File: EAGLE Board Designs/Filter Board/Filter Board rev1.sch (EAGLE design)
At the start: 9 parts, among them U1 MAX7400

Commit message: progress
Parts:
- removed U1: MAX7400, HyTechDevices:MAX7400
- added C2: CAPACITOR_0603_25V_47NF, HyTechDevices:CAPACITOR_0603_25V_47NF
- added J4, J5: CONNECTOR-40__, HyTechDevices:CONNECTOR-40__
- added R5: RESISTOR_0603_3.3K, HyTechDevices:RESISTOR_0603_3.3K
- C1: value CAPACITOR_0603_10V_680PF -> CAPACITOR_0603_25V_47NF; device HyTechDevices:CAPACITOR_0603_10V_680PF -> HyTechDevices:CAPACITOR_0603_25V_47NF
- C3: value (none) -> CAPACITOR_0603_25V_47NF; device HyTechSymbols:CAPACITOR -> HyTechDevices:CAPACITOR_0603_25V_47NF
- C5: value CAPACITOR_0603_10V_0.1UF -> CAPACITOR_0603_25V_47NF; device HyTechDevices:CAPACITOR_0603_10V_0.1UF -> HyTechDevices:CAPACITOR_0603_25V_47NF
- R1: value (none) -> RESISTOR_0603_3.3K; device HyTechSymbols:RESISTOR -> HyTechDevices:RESISTOR_0603_3.3K
- R2: value RESISTOR_0603_13K -> RESISTOR_0603_3.3K; device HyTechDevices:RESISTOR_0603_13K -> HyTechDevices:RESISTOR_0603_3.3K
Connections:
- removed net FILTERED_FREQ: C3.1, R1.2
- removed net INPUT_SIGNAL: U1.IN
- removed net N$3: C1.1, U1.CLK
- removed net N$4: C5.1, U1.COM, U1.OS
- removed net OUTPUT_SIGNAL: U1.OUT
- removed net RAW_24V_SIGNAL: R2.1
- removed net REGULATED_SIGNAL: R2.2, R3.1
- new net ACCEL_1: J5.5
- new net ACCEL_1_EXT: J5.3
- new net ACCEL_2: J5.9
- new net ACCEL_2_EXT: J5.7
- new net BRAKE_1: J5.13
- new net BRAKE_1_EXT: J5.11
- new net BRAKE_2: J5.17
- new net BRAKE_2_EXT: J5.15
- new net BRAKE_PRESSURE_F: C2.1, J5.28, R2.2
- new net BRAKE_PRESSURE_F_EXT: J5.27, R2.1
- new net BRAKE_PRESSURE_R: C3.1, J5.30, R3.2
- new net BRAKE_PRESSURE_R_EXT: J5.29, R3.1
- new net CURRENT: J5.34
- new net CURRENT_EXT: J5.32
- new net LOAD_FL: J4.5
- new net LOAD_FL_EXT: J4.3
- new net LOAD_FR: J4.9
- new net LOAD_FR_EXT: J4.7
- new net LOAD_RL: J4.13
- new net LOAD_RL_EXT: J4.11
- new net LOAD_RR: J4.17
- new net LOAD_RR_EXT: J4.15
- new net REFERENCE: J5.38
- new net REFERENCE_EXT: J5.36
- new net SPN_POT_1: J4.21
- new net SPN_POT_1_EXT: J4.19
- new net SPN_POT_2: J4.25
- new net SPN_POT_2_EXT: J4.23
- new net SPN_POT_3: J4.29
- new net SPN_POT_3_EXT: J4.27
- new net SPN_POT_4: J4.33
- new net SPN_POT_4_EXT: J4.31
- new net SPN_POT_5: J4.37
- new net SPN_POT_5_EXT: J4.35
- new net SPN_POT_6: J5.1
- new net SPN_POT_6_EXT: J4.39
- new net STEERING_1: C5.1, J5.21, R5.2
- new net STEERING_1_EXT: J5.19, R5.1
- new net STEERING_2: C1.1, J5.25, R1.2
- new net STEERING_2_EXT: J5.23, R1.1
- net +5V: now also J4.1; no longer U1.!SHDN, U1.VDD
- net GND: now also C2.2, J4.10, J4.12, J4.14, J4.16, J4.18, J4.2, J4.20, J4.22, J4.24, J4.26, J4.28, J4.30, J4.32, J4.34, J4.36, J4.38, J4.4, J4.6, J4.8, J5.10, J5.12, J5.14, J5.16, J5.18, J5.2, J5.20, J5.22, J5.24, J5.26, J5.31, J5.33, J5.35, J5.37, J5.4, J5.6, J5.8; no longer R3.2, U1.GND
- net REGULATED_FREQ: no longer R1.1
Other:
- moved on the sheet: C1, C3, C5, C6, C7, R1, R2, R3

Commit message: Prototype filter schematic
my eagle is scuffed :(
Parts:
- added C10, C14, C18, C22, C58, C62, C66, C70, C74, C78: CAPACITOR_0603_10V_1UF, HyTechDevices:CAPACITOR_0603_10V_1UF
- added C11, C13, C15, C17, C19, C21, C23, C4, C55, C57, C59, C61, C63, C65, C67, C69, C71, C73, C75, C77, C79, C9: CAPACITOR_0603_10V_0.1UF, HyTechDevices:CAPACITOR_0603_10V_0.1UF
- added C12, C16, C20, C24, C56, C60, C64, C68, C72, C76, C8, C80: CAPACITOR_0603_10V_680PF, HyTechDevices:CAPACITOR_0603_10V_680PF
- added C49, C50, C51, C52, C53, C54: CAPACITOR_0603_25V_47NF, HyTechDevices:CAPACITOR_0603_25V_47NF
- added R10, R12, R14, R16, R18, R19, R20, R21, R22, R23, R24, R26, R30, R32, R34, R6, R8: RESISTOR_0603_3.3K, HyTechDevices:RESISTOR_0603_3.3K
- added R11, R13, R15, R17, R25, R29, R31, R33, R4, R7, R9: RESISTOR_0603_13K, HyTechDevices:RESISTOR_0603_13K
- added U1, U12, U13, U14, U15, U16, U17, U18, U2, U3, U4, U5: MAX7400, HyTechDevices:MAX7400
- C1: value CAPACITOR_0603_25V_47NF -> CAPACITOR_0603_10V_0.1UF; device HyTechDevices:CAPACITOR_0603_25V_47NF -> HyTechDevices:CAPACITOR_0603_10V_0.1UF
- C5: value CAPACITOR_0603_25V_47NF -> CAPACITOR_0603_10V_1UF; device HyTechDevices:CAPACITOR_0603_25V_47NF -> HyTechDevices:CAPACITOR_0603_10V_1UF
- R1: value RESISTOR_0603_3.3K -> RESISTOR_0603_13K; device HyTechDevices:RESISTOR_0603_3.3K -> HyTechDevices:RESISTOR_0603_13K
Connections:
- new net CURRENT_EXT_5V: R1.2, R5.1, U18.IN
- new net GND1: R12.2, R16.2
- new net GND2: R14.2, R18.2, R26.2, R5.2
- new net LOAD_FL_EXT_5V: R29.2, R30.1, U2.IN
- new net LOAD_FR_EXT_5V: R7.2, R8.1, U3.IN
- new net LOAD_RL_EXT_5V: R31.2, R32.1, U4.IN
- new net LOAD_RR_EXT_5V: R33.2, R34.1, U5.IN
- new net N$10: C19.1, U4.COM, U4.OS
- new net N$11: C24.1, U5.CLK
- new net N$12: C23.1, U5.COM, U5.OS
- new net N$25: C56.1, U12.CLK
- new net N$26: C55.1, U12.COM, U12.OS
- new net N$27: C64.1, U14.CLK
- new net N$28: C63.1, U14.COM, U14.OS
- new net N$29: C60.1, U13.CLK
- new net N$3: C8.1, U1.CLK
- new net N$30: C59.1, U13.COM, U13.OS
- new net N$31: C72.1, U16.CLK
- new net N$32: C71.1, U16.COM, U16.OS
- new net N$33: C68.1, U15.CLK
- new net N$34: C67.1, U15.COM, U15.OS
- new net N$35: C80.1, U18.CLK
- new net N$36: C79.1, U18.COM, U18.OS
- new net N$37: C76.1, U17.CLK
- new net N$38: C75.1, U17.COM, U17.OS
- new net N$4: C4.1, U1.COM, U1.OS
- new net N$5: C12.1, U2.CLK
- new net N$6: C11.1, U2.COM, U2.OS
- new net N$7: C16.1, U3.CLK
- new net N$8: C15.1, U3.COM, U3.OS
- new net N$9: C20.1, U4.CLK
- new net REFERENCE_EXT_5V: R25.2, R26.1, U1.IN
- new net SPN_POT_1_EXT_5V: R10.1, R22.1, R9.2
- new net SPN_POT_2_EXT_5V: R23.1, R4.2, R6.1
- new net SPN_POT_3_EXT_5V: R15.2, R16.1, R24.1
- new net SPN_POT_4_EXT_5V: R17.2, R18.1, R19.1
- new net SPN_POT_5_EXT_5V: R11.2, R12.1, R20.1
- new net SPN_POT_6_EXT_5V: R13.2, R14.1, R21.1
- net +5V: now also U1.!SHDN, U1.VDD, U12.!SHDN, U12.VDD, U13.!SHDN, U13.VDD, U14.!SHDN, U14.VDD, U15.!SHDN, U15.VDD, U16.!SHDN, U16.VDD, U17.!SHDN, U17.VDD, U18.!SHDN, U18.VDD, U2.!SHDN, U2.VDD, U3.!SHDN, U3.VDD, U4.!SHDN, U4.VDD, U5.!SHDN, U5.VDD
- net ACCEL_1: now also U12.OUT
- net ACCEL_1_EXT: now also U12.IN
- net ACCEL_2: now also U13.OUT
- net ACCEL_2_EXT: now also U13.IN
- net BRAKE_1: now also U14.OUT
- net BRAKE_1_EXT: now also U14.IN
- net BRAKE_2: now also U15.OUT
- net BRAKE_2_EXT: now also U15.IN
- net CURRENT: now also U18.OUT
- net CURRENT_EXT: now also R1.1
- net GND: now also C10.2, C11.2, C12.2, C13.2, C14.2, C15.2, C16.2, C17.2, C18.2, C19.2, C20.2, C21.2, C22.2, C23.2, C24.2, C4.2, C49.2, C50.2, C51.2, C52.2, C53.2, C54.2, C55.2, C56.2, C57.2, C58.2, C59.2, C60.2, C61.2, C62.2, C63.2, C64.2, C65.2, C66.2, C67.2, C68.2, C69.2, C70.2, C71.2, C72.2, C73.2, C74.2, C75.2, C76.2, C77.2, C78.2, C79.2, C8.2, C80.2, C9.2, R10.2, R30.2, R32.2, R34.2, R6.2, R8.2, U1.GND, U12.GND, U13.GND, U14.GND, U15.GND, U16.GND, U17.GND, U18.GND, U2.GND, U3.GND, U4.GND, U5.GND
- net LOAD_FL: now also U2.OUT
- net LOAD_FL_EXT: now also R29.1
- net LOAD_FR: now also U3.OUT
- net LOAD_FR_EXT: now also R7.1
- net LOAD_RL: now also U4.OUT
- net LOAD_RL_EXT: now also R31.1
- net LOAD_RR: now also U5.OUT
- net LOAD_RR_EXT: now also R33.1
- net REFERENCE: now also U1.OUT
- net REFERENCE_EXT: now also R25.1
- net REGULATED_FREQ: now also C1.1, C10.1, C13.1, C14.1, C17.1, C18.1, C21.1, C22.1, C5.1, C57.1, C58.1, C61.1, C62.1, C65.1, C66.1, C69.1, C70.1, C73.1, C74.1, C77.1, C78.1, C9.1
- net SPN_POT_1: now also C52.1, R22.2
- net SPN_POT_1_EXT: now also R9.1
- net SPN_POT_2: now also C53.1, R23.2
- net SPN_POT_2_EXT: now also R4.1
- net SPN_POT_3: now also C54.1, R24.2
- net SPN_POT_3_EXT: now also R15.1
- net SPN_POT_4: now also C49.1, R19.2
- net SPN_POT_4_EXT: now also R17.1
- net SPN_POT_5: now also C50.1, R20.2
- net SPN_POT_5_EXT: now also R11.1
- net SPN_POT_6: now also C51.1, R21.2
- net SPN_POT_6_EXT: now also R13.1
- net STEERING_1: now also U16.OUT; no longer C5.1, R5.2
- net STEERING_1_EXT: now also U16.IN; no longer R5.1
- net STEERING_2: now also U17.OUT; no longer C1.1, R1.2
- net STEERING_2_EXT: now also U17.IN; no longer R1.1

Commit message: Updated Filter Board Schematic
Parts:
- added C100, C104, C28, C32, C36, C40, C44, C48, C84, C88, C92, C96: CAPACITOR_0603_10V_680PF, HyTechDevices:CAPACITOR_0603_10V_680PF
- added C101, C103, C25, C27, C29, C31, C33, C35, C37, C39, C41, C43, C45, C47, C81, C83, C85, C87, C89, C91, C93, C95, C97, C99: CAPACITOR_0603_10V_0.1UF, HyTechDevices:CAPACITOR_0603_10V_0.1UF
- added C102, C26, C30, C34, C38, C42, C46, C82, C86, C90, C94, C98: CAPACITOR_0603_10V_1UF, HyTechDevices:CAPACITOR_0603_10V_1UF
- added R27, R35, R37, R39, R41, R43: RESISTOR_0603_13K, HyTechDevices:RESISTOR_0603_13K
- added R28, R36, R38, R40, R42, R44: RESISTOR_0603_3.3K, HyTechDevices:RESISTOR_0603_3.3K
- added U10, U11, U19, U20, U21, U22, U23, U24, U6, U7, U8, U9: MAX7400, HyTechDevices:MAX7400
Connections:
- new net N$1: C28.1, U6.CLK
- new net N$13: C32.1, U7.CLK
- new net N$14: C31.1, U7.COM, U7.OS
- new net N$15: C36.1, U8.CLK
- new net N$16: C35.1, U8.COM, U8.OS
- new net N$17: C40.1, U9.CLK
- new net N$18: C39.1, U9.COM, U9.OS
- new net N$19: C44.1, U10.CLK
- new net N$2: C27.1, U6.COM, U6.OS
- new net N$20: C43.1, U10.COM, U10.OS
- new net N$21: C48.1, U11.CLK
- new net N$22: C47.1, U11.COM, U11.OS
- new net N$23: C84.1, U19.CLK
- new net N$24: C83.1, U19.COM, U19.OS
- new net N$39: C88.1, U20.CLK
- new net N$40: C87.1, U20.COM, U20.OS
- new net N$41: C92.1, U21.CLK
- new net N$42: C91.1, U21.COM, U21.OS
- new net N$43: C96.1, U22.CLK
- new net N$44: C95.1, U22.COM, U22.OS
- new net N$45: C100.1, U23.CLK
- new net N$46: C99.1, U23.COM, U23.OS
- new net N$47: C104.1, U24.CLK
- new net N$48: C103.1, U24.COM, U24.OS
- net +5V: now also U10.!SHDN, U10.VDD, U11.!SHDN, U11.VDD, U19.!SHDN, U19.VDD, U20.!SHDN, U20.VDD, U21.!SHDN, U21.VDD, U22.!SHDN, U22.VDD, U23.!SHDN, U23.VDD, U24.!SHDN, U24.VDD, U6.!SHDN, U6.VDD, U7.!SHDN, U7.VDD, U8.!SHDN, U8.VDD, U9.!SHDN, U9.VDD
- net ACCEL_1: now also U8.OUT
- net ACCEL_1_EXT: now also U8.IN
- net ACCEL_2: now also U21.OUT
- net ACCEL_2_EXT: now also U21.IN
- net BRAKE_1: now also U19.OUT
- net BRAKE_1_EXT: now also U19.IN
- net BRAKE_2: now also U22.OUT
- net BRAKE_2_EXT: now also U22.IN
- net CURRENT: now also U11.OUT
- net CURRENT_EXT: now also R41.1
- net CURRENT_EXT_5V: now also R41.2, R42.1, U11.IN
- net GND: now also C100.2, C101.2, C102.2, C103.2, C104.2, C25.2, C26.2, C27.2, C28.2, C29.2, C30.2, C31.2, C32.2, C33.2, C34.2, C35.2, C36.2, C37.2, C38.2, C39.2, C40.2, C41.2, C42.2, C43.2, C44.2, C45.2, C46.2, C47.2, C48.2, C81.2, C82.2, C83.2, C84.2, C85.2, C86.2, C87.2, C88.2, C89.2, C90.2, C91.2, C92.2, C93.2, C94.2, C95.2, C96.2, C97.2, C98.2, C99.2, R28.2, R36.2, R38.2, R40.2, U10.GND, U11.GND, U19.GND, U20.GND, U21.GND, U22.GND, U23.GND, U24.GND, U6.GND, U7.GND, U8.GND, U9.GND
- net GND2: now also R42.2, R44.2
- net LOAD_FL: now also U9.OUT
- net LOAD_FL_EXT: now also R37.1
- net LOAD_FL_EXT_5V: now also R37.2, R38.1, U9.IN
- net LOAD_FR: now also U10.OUT
- net LOAD_FR_EXT: now also R39.1
- net LOAD_FR_EXT_5V: now also R39.2, R40.1, U10.IN
- net LOAD_RL: now also U6.OUT
- net LOAD_RL_EXT: now also R27.1
- net LOAD_RL_EXT_5V: now also R27.2, R28.1, U6.IN
- net LOAD_RR: now also U7.OUT
- net LOAD_RR_EXT: now also R35.1
- net LOAD_RR_EXT_5V: now also R35.2, R36.1, U7.IN
- net REFERENCE: now also U24.OUT
- net REFERENCE_EXT: now also R43.1
- net REFERENCE_EXT_5V: now also R43.2, R44.1, U24.IN
- net REGULATED_FREQ: now also C101.1, C102.1, C25.1, C26.1, C29.1, C30.1, C33.1, C34.1, C37.1, C38.1, C41.1, C42.1, C45.1, C46.1, C81.1, C82.1, C85.1, C86.1, C89.1, C90.1, C93.1, C94.1, C97.1, C98.1
- net STEERING_1: now also U20.OUT
- net STEERING_1_EXT: now also U20.IN
- net STEERING_2: now also U23.OUT
- net STEERING_2_EXT: now also U23.IN

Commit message: added second order rc filter
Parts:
- removed C11, C13, C15, C17, C19, C21, C23, C55, C57, C59, C61, C63, C65, C67, C69, C71, C73, C75, C77, C79: CAPACITOR_0603_10V_0.1UF, HyTechDevices:CAPACITOR_0603_10V_0.1UF
- removed C12, C16, C20, C24, C56, C60, C64, C68, C72, C76, C80: CAPACITOR_0603_10V_680PF, HyTechDevices:CAPACITOR_0603_10V_680PF
- removed C14, C18, C22, C58, C62, C66, C70, C74, C78: CAPACITOR_0603_10V_1UF, HyTechDevices:CAPACITOR_0603_10V_1UF
- removed R31, R33: RESISTOR_0603_13K, HyTechDevices:RESISTOR_0603_13K
- removed R32, R34: RESISTOR_0603_3.3K, HyTechDevices:RESISTOR_0603_3.3K
- removed U1, U12, U13, U14, U15, U16, U17, U18, U2, U3, U4, U5: MAX7400, HyTechDevices:MAX7400
- C1, C4, C6, C9: value CAPACITOR_0603_10V_0.1UF -> CAPACITOR_0603_25V_47NF; device HyTechDevices:CAPACITOR_0603_10V_0.1UF -> HyTechDevices:CAPACITOR_0603_25V_47NF
- C10, C5, C7: value CAPACITOR_0603_10V_1UF -> CAPACITOR_0603_25V_47NF; device HyTechDevices:CAPACITOR_0603_10V_1UF -> HyTechDevices:CAPACITOR_0603_25V_47NF
- C8: value CAPACITOR_0603_10V_680PF -> CAPACITOR_0603_25V_47NF; device HyTechDevices:CAPACITOR_0603_10V_680PF -> HyTechDevices:CAPACITOR_0603_25V_47NF
- R1, R25, R29, R7: value RESISTOR_0603_13K -> RESISTOR_0603_3.3K; device HyTechDevices:RESISTOR_0603_13K -> HyTechDevices:RESISTOR_0603_3.3K
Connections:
- removed net N$12: C23.1, U5.COM, U5.OS
- removed net N$25: C56.1, U12.CLK
- removed net N$26: C55.1, U12.COM, U12.OS
- removed net N$27: C64.1, U14.CLK
- removed net N$28: C63.1, U14.COM, U14.OS
- removed net N$29: C60.1, U13.CLK
- removed net N$30: C59.1, U13.COM, U13.OS
- removed net N$31: C72.1, U16.CLK
- removed net N$32: C71.1, U16.COM, U16.OS
- removed net N$33: C68.1, U15.CLK
- removed net N$34: C67.1, U15.COM, U15.OS
- removed net N$35: C80.1, U18.CLK
- removed net N$36: C79.1, U18.COM, U18.OS
- removed net N$37: C76.1, U17.CLK
- removed net N$38: C75.1, U17.COM, U17.OS
- net +5V: no longer U1.!SHDN, U1.VDD, U12.!SHDN, U12.VDD, U13.!SHDN, U13.VDD, U14.!SHDN, U14.VDD, U15.!SHDN, U15.VDD, U16.!SHDN, U16.VDD, U17.!SHDN, U17.VDD, U18.!SHDN, U18.VDD, U2.!SHDN, U2.VDD, U3.!SHDN, U3.VDD, U4.!SHDN, U4.VDD, U5.!SHDN, U5.VDD
- net ACCEL_1: no longer U12.OUT
- net ACCEL_1_EXT: no longer U12.IN
- net ACCEL_2: no longer U13.OUT
- net ACCEL_2_EXT: no longer U13.IN
- net BRAKE_1: no longer U14.OUT
- net BRAKE_1_EXT: no longer U14.IN
- net BRAKE_2: no longer U15.OUT
- net BRAKE_2_EXT: no longer U15.IN
- net BRAKE_PRESSURE_F: now also C9.1, R29.2; no longer C2.1, R2.2
- net BRAKE_PRESSURE_R: now also C10.1, R30.2; no longer C3.1, R3.2
- net CURRENT: no longer U18.OUT
- net CURRENT_EXT: no longer R1.1
- net CURRENT_EXT_5V: no longer R1.2, R5.1, U18.IN
- net GND: no longer C11.2, C12.2, C13.2, C14.2, C15.2, C16.2, C17.2, C18.2, C19.2, C20.2, C21.2, C22.2, C23.2, C24.2, C55.2, C56.2, C57.2, C58.2, C59.2, C60.2, C61.2, C62.2, C63.2, C64.2, C65.2, C66.2, C67.2, C68.2, C69.2, C70.2, C71.2, C72.2, C73.2, C74.2, C75.2, C76.2, C77.2, C78.2, C79.2, C80.2, R30.2, R32.2, R34.2, R8.2, U1.GND, U12.GND, U13.GND, U14.GND, U15.GND, U16.GND, U17.GND, U18.GND, U2.GND, U3.GND, U4.GND, U5.GND
- net GND2: no longer R26.2, R5.2
- net LOAD_FL: no longer U2.OUT
- net LOAD_FL_EXT: no longer R29.1
- net LOAD_FL_EXT_5V: no longer R29.2, R30.1, U2.IN
- net LOAD_FR: no longer U3.OUT
- net LOAD_FR_EXT: no longer R7.1
- net LOAD_FR_EXT_5V: no longer R7.2, R8.1, U3.IN
- net LOAD_RL: no longer U4.OUT
- net LOAD_RL_EXT: no longer R31.1
- net LOAD_RL_EXT_5V: no longer R31.2, R32.1, U4.IN
- net LOAD_RR: no longer U5.OUT
- net LOAD_RR_EXT: no longer R33.1
- net LOAD_RR_EXT_5V: no longer R33.2, R34.1, U5.IN
- net N$10: now also C2.1, R2.2, R29.1; no longer C19.1, U4.COM, U4.OS
- net N$11: now also R30.1; no longer C24.1, U5.CLK
- net N$3: now also C3.1, R3.2; no longer C8.1, U1.CLK
- net N$4: now also C52.1, R1.1, R22.2; no longer C4.1, U1.COM, U1.OS
- net N$5: now also C49.1, R19.2, R5.1; no longer C12.1, U2.CLK
- net N$6: now also C50.1, R20.2, R7.1; no longer C11.1, U2.COM, U2.OS
- net N$7: now also C51.1, R21.2, R8.1; no longer C16.1, U3.CLK
- net N$8: now also C54.1, R24.2, R25.1; no longer C15.1, U3.COM, U3.OS
- net N$9: now also C53.1, R23.2, R26.1; no longer C20.1, U4.CLK
- net REFERENCE: no longer U1.OUT
- net REFERENCE_EXT: no longer R25.1
- net REFERENCE_EXT_5V: no longer R25.2, R26.1, U1.IN
- net REGULATED_FREQ: no longer C1.1, C10.1, C13.1, C14.1, C17.1, C18.1, C21.1, C22.1, C5.1, C57.1, C58.1, C6.1, C61.1, C62.1, C65.1, C66.1, C69.1, C7.1, C70.1, C73.1, C74.1, C77.1, C78.1, C9.1
- net SPN_POT_1: now also C1.1, R1.2; no longer C52.1, R22.2
- net SPN_POT_2: now also C8.1, R26.2; no longer C53.1, R23.2
- net SPN_POT_3: now also C7.1, R25.2; no longer C54.1, R24.2
- net SPN_POT_4: now also C4.1, R5.2; no longer C49.1, R19.2
- net SPN_POT_5: now also C5.1, R7.2; no longer C50.1, R20.2
- net SPN_POT_6: now also C6.1, R8.2; no longer C51.1, R21.2
- net STEERING_1: no longer U16.OUT
- net STEERING_1_EXT: no longer U16.IN
- net STEERING_2: no longer U17.OUT
- net STEERING_2_EXT: no longer U17.IN
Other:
- moved on the sheet: C1, C10, C4, C5, C6, C7, C8, C9, R1, R25, R26, R29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

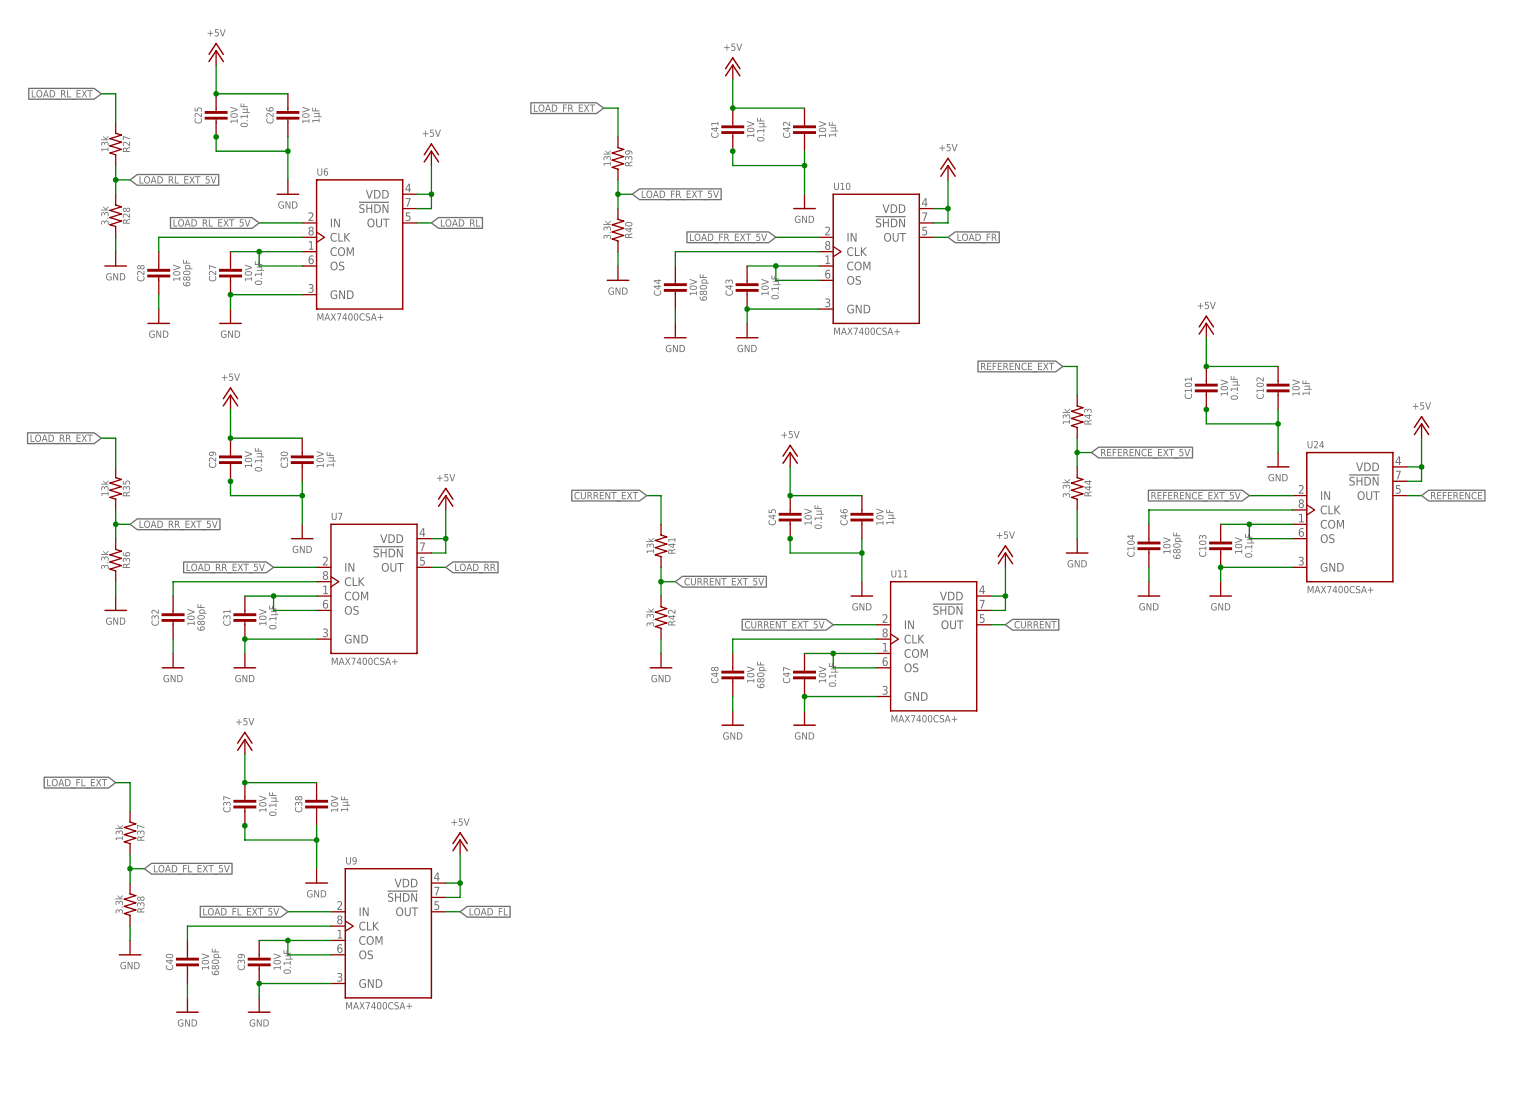
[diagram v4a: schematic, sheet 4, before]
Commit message: Grouped components together!
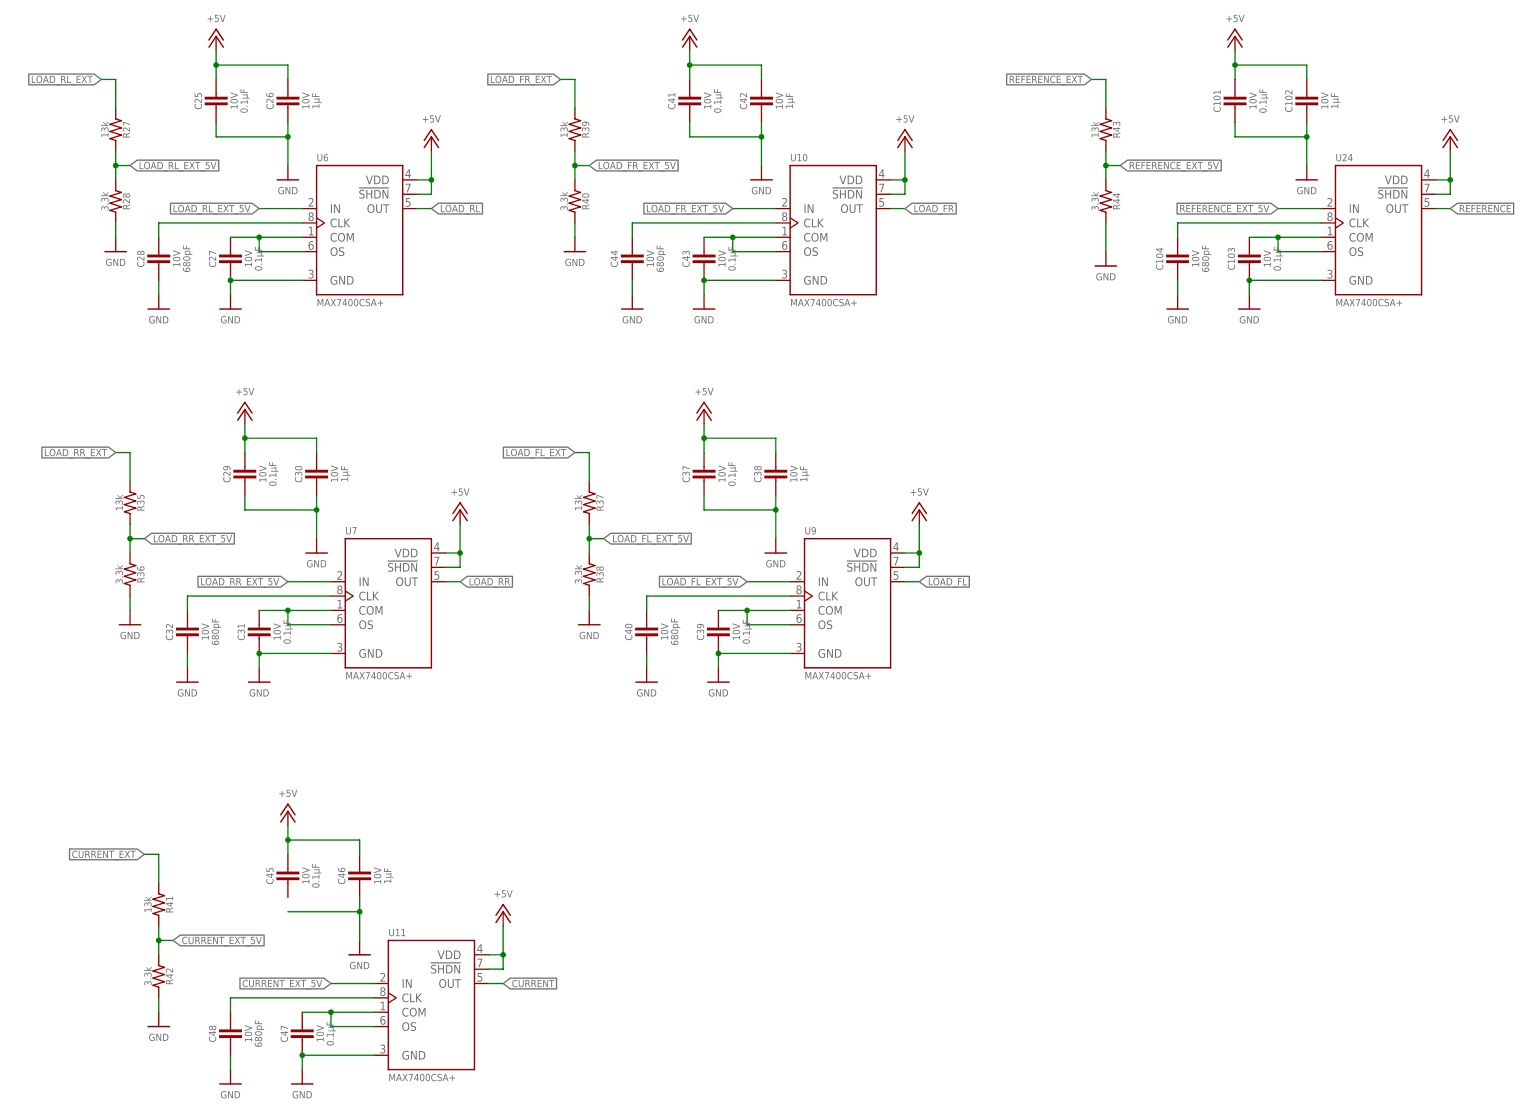
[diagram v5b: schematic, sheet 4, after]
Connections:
- removed net N$3: C3.1, R3.2
- removed net REGULATED_FREQ: C101.1, C102.1, C25.1, C26.1, C29.1, C30.1, C33.1, C34.1, C37.1, C38.1, C41.1, C42.1, C45.1, C46.1, C81.1, C82.1, C85.1, C86.1, C89.1, C90.1, C93.1, C94.1, C97.1, C98.1
- net +5V: now also C101.1, C102.1, C25.1, C26.1, C29.1, C30.1, C33.1, C34.1, C37.1, C38.1, C41.1, C42.1, C45.1, C46.1, C81.1, C82.1, C85.1, C86.1, C89.1, C90.1, C93.1, C94.1, C97.1, C98.1
- net GND: no longer C45.2
- net N$11: now also C3.1, R3.2
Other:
- moved on the sheet: C101, C102, C103, C104, C25, C26, C27, C28, C29, C30, C31, C32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

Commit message: quick fix
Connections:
- net GND: now also C45.2
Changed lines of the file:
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@@
 <pinref part="P139" gate="1" pin="GND"/>
 <pinref part="C46" gate="G$1" pin="2"/>
+<pinref part="C45" gate="G$1" pin="2"/>
+<wire x1="55.88" y1="53.34" x2="55.88" y2="50.8" width="0.1524" layer="91"/>
 </segment>
 <segment>
